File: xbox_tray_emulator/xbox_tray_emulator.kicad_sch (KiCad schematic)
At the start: 4 parts, among them J1 to Xbox, U1 ATtiny13A-S

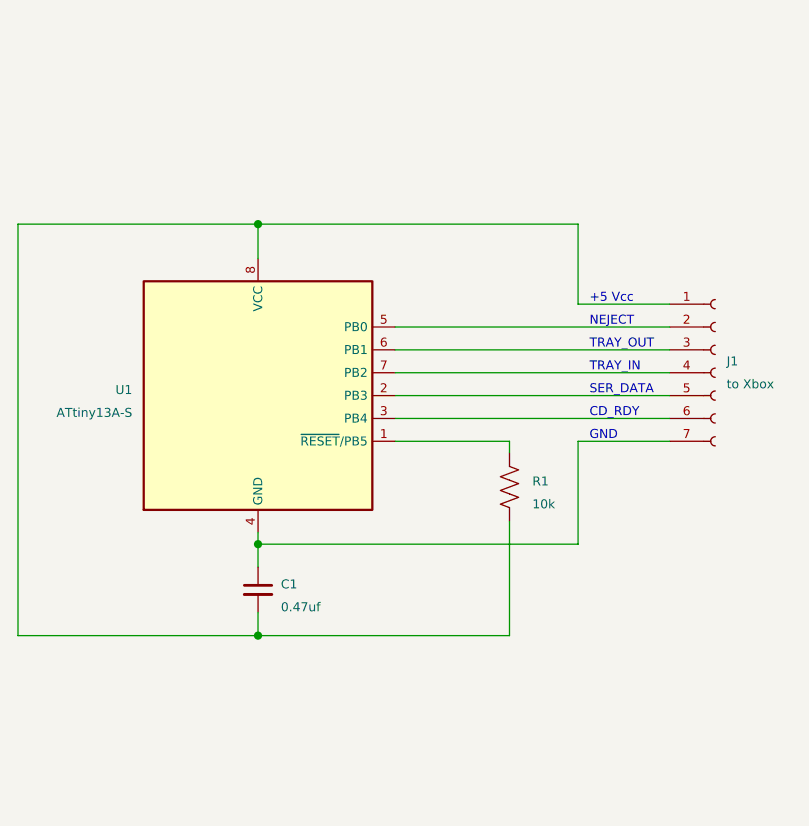
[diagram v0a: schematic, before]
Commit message: modify for ATtiny13A
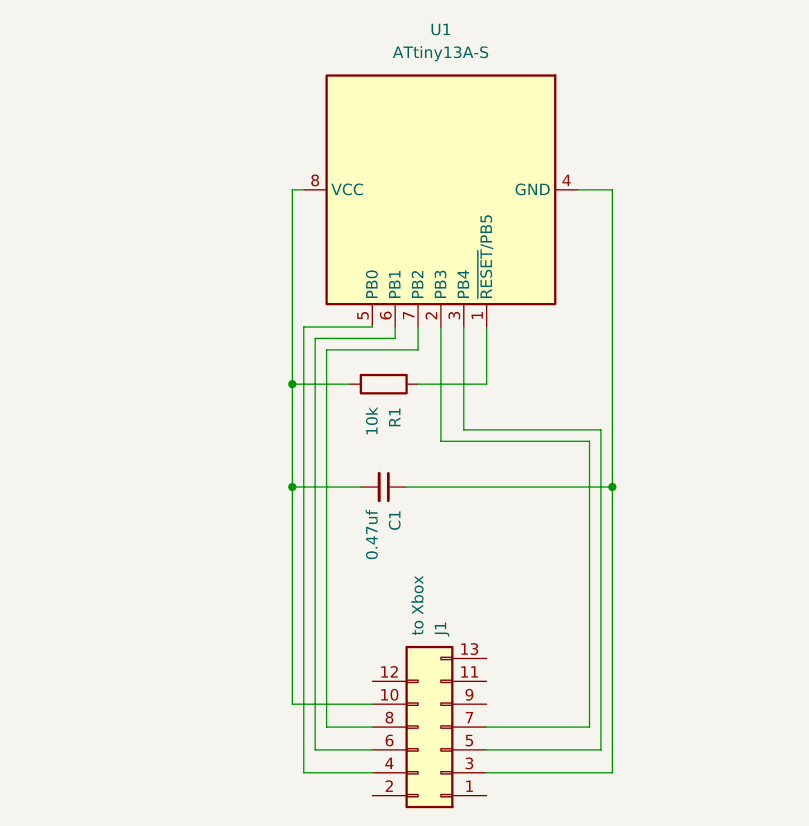
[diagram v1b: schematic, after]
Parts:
- removed J1: to Xbox, symbol Connector:Conn_01x07_Female
- removed R1: 10k, symbol Device:R_US
- added J1: to Xbox, Connector_Hirose:Hirose_DF11-14DP-2DSA_2x07_P2.00mm_Vertical, symbol Connector_Generic:Conn_2Rows-13Pins
- added R1: 10k, Resistor_SMD:R_0805_2012Metric_Pad1.20x1.40mm_HandSolder, symbol Device:R
- C1: footprint (none) -> Capacitor_SMD:C_0805_2012Metric_Pad1.18x1.45mm_HandSolder
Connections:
- net at U1.1 (~{RESET}/PB5): now also R1.1
- net at C1.2, U1.8 (VCC): now also J1.10 (Pin_10), R1.2
- net at C1.1, U1.4 (GND): now also J1.3 (Pin_3)
- net at U1.2 (PB3): now also J1.7 (Pin_7)
- net at U1.3 (PB4): now also J1.5 (Pin_5)
- net at U1.5 (PB0): now also J1.4 (Pin_4)
- net at U1.6 (PB1): now also J1.6 (Pin_6)
- net at U1.7 (PB2): now also J1.8 (Pin_8)
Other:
- note removed: "+5 Vcc"
- note removed: "CD_RDY"
- note removed: "GND"
- note removed: "NEJECT"
- note removed: "SER_DATA"
- note removed: "TRAY_IN"
- note removed: "TRAY_OUT"
- moved on the sheet: C1, U1

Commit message: add PCB
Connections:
- net at J1.11 (Pin_11): now also C1.1, J1.12 (Pin_12), J1.3 (Pin_3), U1.4 (GND)
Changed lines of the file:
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@@
 (kicad_sch (version 20211123) (generator eeschema)
   (paper "A4")
+  (junction (at 176.53 129.54) (diameter 0) (color 0 0 0 0)
+  )
+  (junction (at 176.53 139.7) (diameter 0) (color 0 0 0 0)
+  )
   (junction (at 153.67 96.52) (diameter 0) (color 0 0 0 0)
   )
@@
     (stroke (width 0) (type default) (color 0 0 0 0))
   )
+  (wire (pts (xy 176.53 139.7) (xy 176.53 129.54))
+    (stroke (width 0) (type default) (color 0 0 0 0))
+  )
   (wire (pts (xy 175.26 96.52) (xy 175.26 90.17))
     (stroke (width 0) (type default) (color 0 0 0 0))
@@
     (stroke (width 0) (type default) (color 0 0 0 0))
   )
+  (wire (pts (xy 176.53 121.92) (xy 162.56 121.92))
+    (stroke (width 0) (type default) (color 0 0 0 0))
+  )
   (wire (pts (xy 157.48 92.71) (xy 157.48 134.62))
+    (stroke (width 0) (type default) (color 0 0 0 0))
+  )
+  (wire (pts (xy 176.53 139.7) (xy 175.26 139.7))
     (stroke (width 0) (type default) (color 0 0 0 0))
   )
@@
     (stroke (width 0) (type default) (color 0 0 0 0))
   )
+  (wire (pts (xy 162.56 121.92) (xy 162.56 129.54))
+    (stroke (width 0) (type default) (color 0 0 0 0))
+  )
+  (wire (pts (xy 176.53 129.54) (xy 176.53 121.92))
+    (stroke (width 0) (type default) (color 0 0 0 0))
+  )
   (wire (pts (xy 157.48 134.62) (xy 162.56 134.62))
     (stroke (width 0) (type default) (color 0 0 0 0))
@@
   )
   (wire (pts (xy 153.67 107.95) (xy 153.67 132.08))
+    (stroke (width 0) (type default) (color 0 0 0 0))
+  )
+  (wire (pts (xy 176.53 129.54) (xy 175.26 129.54))
     (stroke (width 0) (type default) (color 0 0 0 0))
   )
@@
     (stroke (width 0) (type default) (color 0 0 0 0))
   )
-  (wire (pts (xy 189.23 139.7) (xy 175.26 139.7))
+  (wire (pts (xy 189.23 139.7) (xy 176.53 139.7))
     (stroke (width 0) (type default) (color 0 0 0 0))
   )
@@
     )
     (property "Value" "to Xbox" (id 1) (at 167.6401 124.46 90)
-      (effects (font (size 1.27 1.27)) (justify right))
+      (effects (font (size 1.27 1.27)) (justify right) hide)
     )
     (property "Footprint" "Connector_Hirose:Hirose_DF11-14DP-2DSA_2x07_P2.00mm_Vertical" (id 2) (at 170.18 134.62 0)

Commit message: PCB cleanup
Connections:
- net at C1.2, J1.10 (Pin_10), R1.2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: now also J1.2 (Pin_2)
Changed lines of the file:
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@@
   (junction (at 153.67 107.95) (diameter 0) (color 0 0 0 0)
+  )
+  (junction (at 153.67 132.08) (diameter 0) (color 0 0 0 0)
   )
   (wire (pts (xy 186.69 102.87) (xy 186.69 134.62))
@@
     (stroke (width 0) (type default) (color 0 0 0 0))
   )
+  (wire (pts (xy 153.67 142.24) (xy 162.56 142.24))
+    (stroke (width 0) (type default) (color 0 0 0 0))
+  )
+  (wire (pts (xy 153.67 132.08) (xy 153.67 142.24))
+    (stroke (width 0) (type default) (color 0 0 0 0))
+  )
